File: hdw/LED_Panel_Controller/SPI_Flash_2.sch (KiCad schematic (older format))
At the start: 14 parts

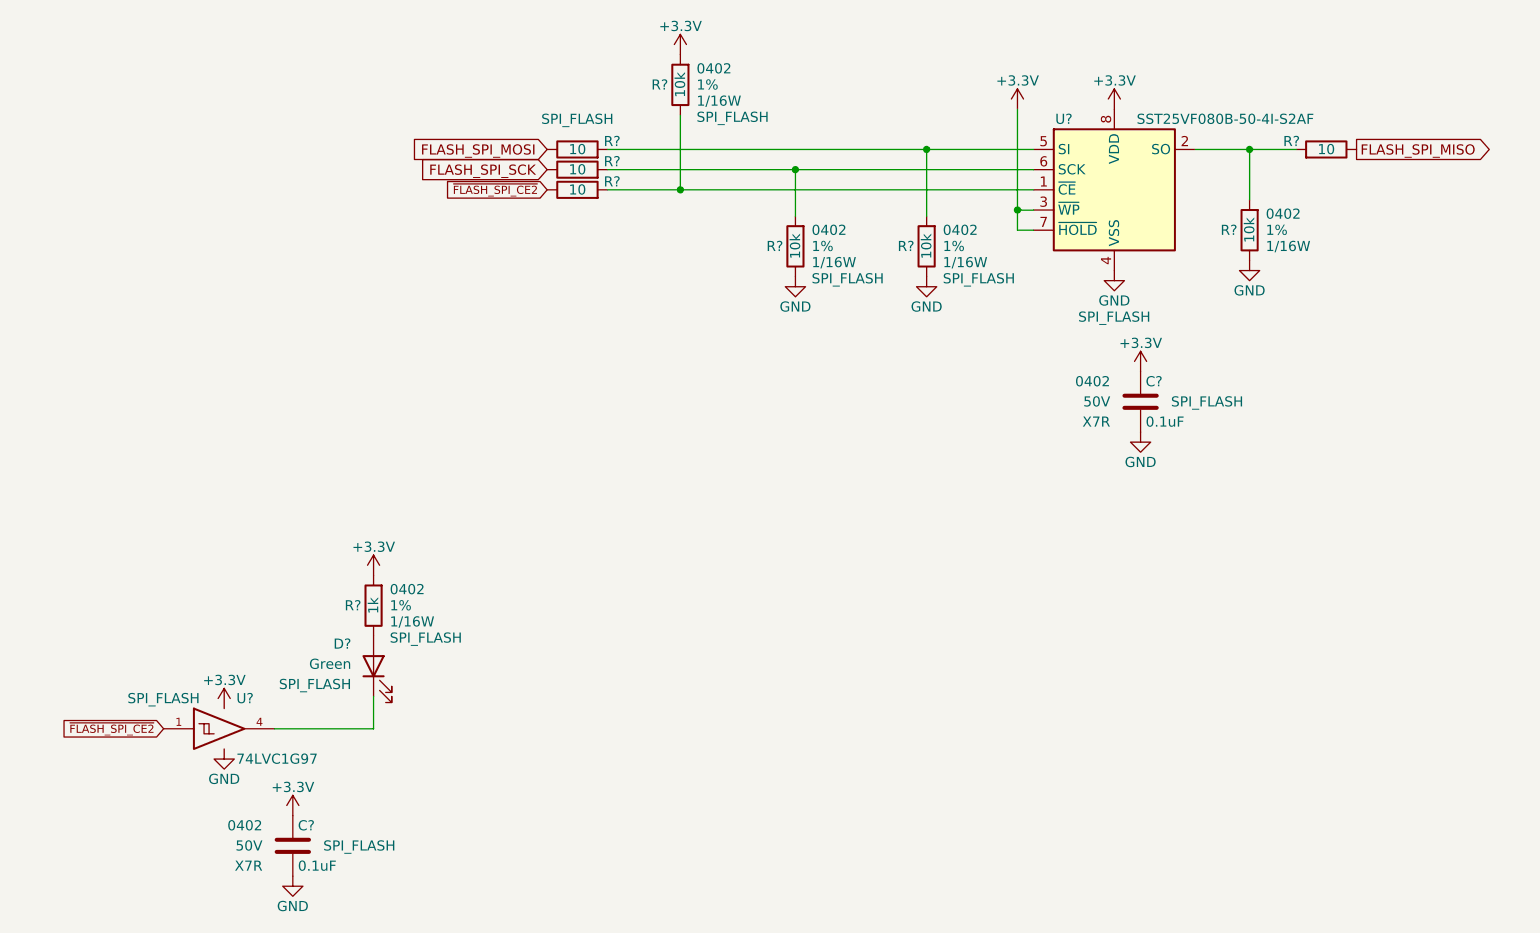
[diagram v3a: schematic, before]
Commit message: assigned I2C addresses
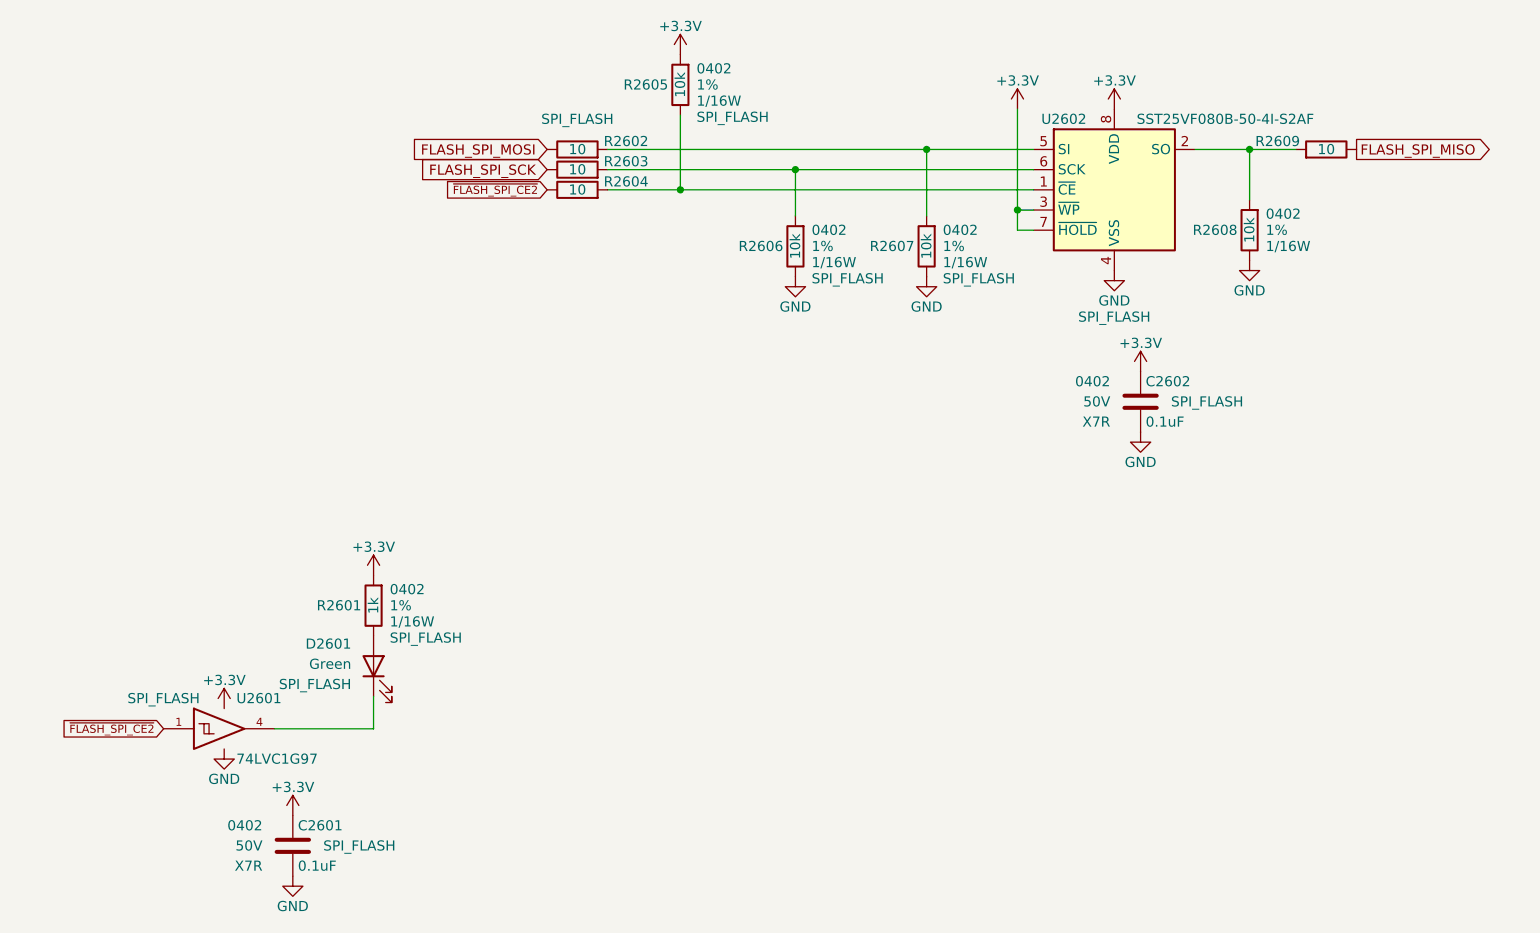
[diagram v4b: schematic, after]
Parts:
- removed C? (x2): 0.1uF, Capacitors_SMD:C_0402, symbol Custom_Library:C_Custom
- removed D?: Green, LEDs:LED_0402, symbol Device:LED
- removed R? (x2): 10k, Resistors_SMD:R_0402, symbol Custom_Library:R_Custom
- removed R? (x2): 10, Resistors_SMD:R_0402, symbol Custom_Library:R_Custom
- removed R?: 1k, Resistors_SMD:R_0402, symbol Custom_Library:R_Custom
- removed U?: SST25VF080B-50-4I-S2AF, Package_SO:SOIC-8_5.275x5.275mm_P1.27mm, symbol Memory_Flash:SST25VF080B-50-4x-S2Ax
- removed U?: 74LVC1G97, Package_TO_SOT_SMD:SOT-363_SC-70-6, symbol Custom_Library:74LVC1G97_Power_BUF
- added C2601, C2602: 0.1uF, Capacitors_SMD:C_0402, symbol Custom_Library:C_Custom
- added D2601: Green, LEDs:LED_0402, symbol Device:LED
- added R2601: 1k, Resistors_SMD:R_0402, symbol Custom_Library:R_Custom
- added R2604, R2609: 10, Resistors_SMD:R_0402, symbol Custom_Library:R_Custom
- added R2605, R2608: 10k, Resistors_SMD:R_0402, symbol Custom_Library:R_Custom
- added U2601: 74LVC1G97, Package_TO_SOT_SMD:SOT-363_SC-70-6, symbol Custom_Library:74LVC1G97_Power_BUF
- added U2602: SST25VF080B-50-4I-S2AF, Package_SO:SOIC-8_5.275x5.275mm_P1.27mm, symbol Memory_Flash:SST25VF080B-50-4x-S2Ax
- gave numbers to parts that had none: 4
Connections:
- net +3V3: now also C2601.1, C2602.1, R2601.1, R2605.1, U2601.5 (VCC), U2602.3 (~WP~), U2602.7 (~HOLD~), U2602.8 (VDD)
- net FLASH_SPI_MISO: now also R2609.2
- net GND: now also C2601.2, C2602.2, R2608.2, U2601.2 (GND), U2601.3 (GND), U2601.6 (GND), U2602.4 (VSS)
- net ~FLASH_SPI_CE2: now also R2604.2, U2601.1
- net at R2602.1, R2607.1: now also U2602.5 (SI)
- net at R2603.1, R2606.1: now also U2602.6 (SCK)
- new net: R2608.1, R2609.1, U2602.2 (SO)
- new net: D2601.1 (K), U2601.4
- new net: D2601.2 (A), R2601.2
- new net: R2604.1, R2605.2, U2602.1 (~CE)
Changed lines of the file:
@@
 $EndDescr
 $Comp
-L power:GND #PWR?
-U 1 1 5BB4E0E3
+L power:GND #PWR02611
+U 1 1 60786261
 P 6080 4050
-F 0 "#PWR?" H 6080 3800 50  0001 C CNN
+F 0 "#PWR02611" H 6080 3800 50  0001 C CNN
 F 1 "GND" H 6080 3900 50  0000 C CNN
 F 2 "" H 6080 4050 50  0001 C CNN
@@
 $EndComp
 $Comp
-L Custom_Library:R_Custom R?
-U 1 1 5BB4EDD1
+L Custom_Library:R_Custom R2608
+U 1 1 6078626A
 P 6750 3850
-F 0 "R?" H 6690 3850 50  0000 R CNN
+F 0 "R2608" H 6690 3850 50  0000 R CNN
 F 1 "10k" V 6750 3850 50  0000 C CNN
 F 2 "Resistors_SMD:R_0402" H 6750 3850 50  0001 C CNN
@@
 $EndComp
 $Comp
-L power:GND #PWR?
-U 1 1 5BB4EE63
+L power:GND #PWR02608
+U 1 1 6078626C
 P 5150 4080
-F 0 "#PWR?" H 5150 3830 50  0001 C CNN
+F 0 "#PWR02608" H 5150 3830 50  0001 C CNN
 F 1 "GND" H 5150 3930 50  0000 C CNN
 F 2 "" H 5150 4080 50  0001 C CNN
@@
 $EndComp
 $Comp
-L power:GND #PWR?
+L power:GND #PWR02614
 U 1 1 5BB4EE7C
 P 6750 4000
-F 0 "#PWR?" H 6750 3750 50  0001 C CNN
+F 0 "#PWR02614" H 6750 3750 50  0001 C CNN
 F 1 "GND" H 6750 3850 50  0000 C CNN
 F 2 "" H 6750 4000 50  0001 C CNN
@@
 $EndComp
 $Comp
-L Custom_Library:R_Custom R?
+L Custom_Library:R_Custom R2602
 U 1 1 5BB4F53B
 P 3420 3450
-F 0 "R?" V 3380 3580 50  0000 L CNN
+F 0 "R2602" V 3380 3580 50  0000 L CNN
 F 1 "10" V 3420 3450 50  0000 C CNN
 F 2 "Resistors_SMD:R_0402" H 3420 3450 50  0001 C CNN
@@
 	3570 3650 3930 3650
 $Comp
-L power:+3.3V #PWR?
-U 1 1 5BDF3D33
+L power:+3.3V #PWR02606
+U 1 1 60786285
 P 3930 2980
-F 0 "#PWR?" H 3930 2830 50  0001 C CNN
+F 0 "#PWR02606" H 3930 2830 50  0001 C CNN
 F 1 "+3.3V" H 3930 3120 50  0000 C CNN
 F 2 "" H 3930 2980 50  0001 C CNN
@@
 $EndComp
 $Comp
-L power:+3.3V #PWR?
-U 1 1 5BDF3DF4
+L power:+3.3V #PWR02610
+U 1 1 6078628C
 P 6080 3250
-F 0 "#PWR?" H 6080 3100 50  0001 C CNN
+F 0 "#PWR02610" H 6080 3100 50  0001 C CNN
 F 1 "+3.3V" H 6080 3390 50  0000 C CNN
 F 2 "" H 6080 3250 50  0001 C CNN
@@
 $Comp
 L Custom_Library:C_Custom C?
-U 1 1 5C15F697
+U 1 1 60786294
 P 2010 6900
-AR Path="/5BAAE16C/5C15F697" Ref="C?"  Part="1"
-AR Path="/5BB181D8/5C15F697" Ref="C?"  Part="1"
-AR Path="/5BB2595E/5C15F697" Ref="C?"  Part="1"
-AR Path="/5F583577/5C15F697" Ref="C?"  Part="1"
-AR Path="/5F583592/5C15F697" Ref="C?"  Part="1"
-F 0 "C?" H 2035 7000 50  0000 L CNN
+AR Path="/5BAAE16C/60786294" Ref="C?"  Part="1"
+AR Path="/5BB181D8/60786294" Ref="C?"  Part="1"
+AR Path="/5BB2595E/60786294" Ref="C?"  Part="1"
+AR Path="/5F583577/60786294" Ref="C?"  Part="1"
+AR Path="/5F583592/60786294" Ref="C2601"  Part="1"
+F 0 "C2601" H 2035 7000 50  0000 L CNN
 F 1 "0.1uF" H 2035 6800 50  0000 L CNN
 F 2 "Capacitors_SMD:C_0402" H 2048 6750 50  0001 C CNN
@@
 $EndComp
 $Comp
-L power:+3.3V #PWR?
-U 1 1 5C161B83
+L power:+3.3V #PWR02601
+U 1 1 6078629A
 P 1670 6220
-F 0 "#PWR?" H 1670 6070 50  0001 C CNN
+F 0 "#PWR02601" H 1670 6070 50  0001 C CNN
 F 1 "+3.3V" H 1670 6360 50  0000 C CNN
 F 2 "" H 1670 6220 50  0001 C CNN
@@
 $EndComp
 $Comp
-L power:+3.3V #PWR?
-U 1 1 5C161BE9
+L power:+3.3V #PWR02603
+U 1 1 6078629E
 P 2010 6750
-F 0 "#PWR?" H 2010 6600 50  0001 C CNN
+F 0 "#PWR02603" H 2010 6600 50  0001 C CNN
 F 1 "+3.3V" H 2010 6890 50  0000 C CNN
 F 2 "" H 2010 6750 50  0001 C CNN
@@
 $EndComp
 $Comp
-L power:GND #PWR?
-U 1 1 5C161C44
+L power:GND #PWR02604
+U 1 1 607862A7
 P 2010 7050
-F 0 "#PWR?" H 2010 6800 50  0001 C CNN
+F 0 "#PWR02604" H 2010 6800 50  0001 C CNN
 F 1 "GND" H 2010 6900 50  0000 C CNN
 F 2 "" H 2010 7050 50  0001 C CNN
@@
 $EndComp
 $Comp
-L power:GND #PWR?
-U 1 1 5C161C9F
+L power:GND #PWR02602
+U 1 1 607862AD
 P 1670 6420
-F 0 "#PWR?" H 1670 6170 50  0001 C CNN
+F 0 "#PWR02602" H 1670 6170 50  0001 C CNN
 F 1 "GND" H 1670 6270 50  0000 C CNN
 F 2 "" H 1670 6420 50  0001 C CNN
@@
 $Comp
 L power:+3.3V #PWR?
-U 1 1 5C166A81
+U 1 1 607862B7
 P 2410 5560
-AR Path="/5BB844FD/5C166A81" Ref="#PWR?"  Part="1"
-AR Path="/5BF346B3/5C166A81" Ref="#PWR?"  Part="1"
-AR Path="/5BB2595E/5C166A81" Ref="#PWR?"  Part="1"
-AR Path="/5F583577/5C166A81" Ref="#PWR?"  Part="1"
-AR Path="/5F583592/5C166A81" Ref="#PWR?"  Part="1"
-F 0 "#PWR?" H 2410 5410 50  0001 C CNN
+AR Path="/5BB844FD/607862B7" Ref="#PWR?"  Part="1"
+AR Path="/5BF346B3/607862B7" Ref="#PWR?"  Part="1"
+AR Path="/5BB2595E/607862B7" Ref="#PWR?"  Part="1"
+AR Path="/5F583577/607862B7" Ref="#PWR?"  Part="1"
+AR Path="/5F583592/607862B7" Ref="#PWR02605"  Part="1"
+F 0 "#PWR02605" H 2410 5410 50  0001 C CNN
 F 1 "+3.3V" H 2410 5700 50  0000 C CNN
 F 2 "" H 2410 5560 50  0001 C CNN
@@
 $Comp
 L Device:LED D?
-U 1 1 5C166A95
+U 1 1 607862B8
 P 2410 6010
-AR Path="/5BB844FD/5C166A95" Ref="D?"  Part="1"
-AR Path="/5BF346B3/5C166A95" Ref="D?"  Part="1"
-AR Path="/5BB2595E/5C166A95" Ref="D?"  Part="1"
-AR Path="/5F583577/5C166A95" Ref="D?"  Part="1"
-AR Path="/5F583592/5C166A95" Ref="D?"  Part="1"
-F 0 "D?" V 2520 6120 50  0000 L CNN
+AR Path="/5BB844FD/607862B8" Ref="D?"  Part="1"
+AR Path="/5BF346B3/607862B8" Ref="D?"  Part="1"
+AR Path="/5BB2595E/607862B8" Ref="D?"  Part="1"
+AR Path="/5F583577/607862B8" Ref="D?"  Part="1"
+AR Path="/5F583592/607862B8" Ref="D2601"  Part="1"
+F 0 "D2601" V 2520 6120 50  0000 L CNN
 F 1 "Green" V 2420 6120 50  0000 L CNN
 F 2 "LEDs:LED_0402" H 2410 6010 50  0001 C CNN
@@
 $EndComp
 $Comp
-L Memory_Flash:SST25VF080B-50-4x-S2Ax U?
-U 1 1 5F6879D5
+L Memory_Flash:SST25VF080B-50-4x-S2Ax U2602
+U 1 1 607862FA
 P 6080 3650
-F 0 "U?" H 5830 4000 50  0000 C CNN
+F 0 "U2602" H 5830 4000 50  0000 C CNN
 F 1 "SST25VF080B-50-4I-S2AF" H 6630 4000 50  0000 C CNN
 F 2 "Package_SO:SOIC-8_5.275x5.275mm_P1.27mm" H 6080 2950 50  0001 C CNN
@@
 $EndComp
 $Comp
-L power:+3.3V #PWR?
-U 1 1 5F689292
+L power:+3.3V #PWR02612
+U 1 1 607862FE
 P 6210 4550
-F 0 "#PWR?" H 6210 4400 50  0001 C CNN
+F 0 "#PWR02612" H 6210 4400 50  0001 C CNN
 F 1 "+3.3V" H 6210 4690 50  0000 C CNN
 F 2 "" H 6210 4550 50  0001 C CNN
@@
 $EndComp
 $Comp
-L power:GND #PWR?
+L power:GND #PWR02613
 U 1 1 5F689298
 P 6210 4850
-F 0 "#PWR?" H 6210 4600 50  0001 C CNN
+F 0 "#PWR02613" H 6210 4600 50  0001 C CNN
 F 1 "GND" H 6210 4700 50  0000 C CNN
 F 2 "" H 6210 4850 50  0001 C CNN
@@
 $EndComp
 $Comp
-L power:+3.3V #PWR?
-U 1 1 5F69329F
+L power:+3.3V #PWR02609
+U 1 1 6078630C
 P 5600 3250
-F 0 "#PWR?" H 5600 3100 50  0001 C CNN
+F 0 "#PWR02609" H 5600 3100 50  0001 C CNN
 F 1 "+3.3V" H 5600 3390 50  0000 C CNN
 F 2 "" H 5600 3250 50  0001 C CNN
@@
 	3570 3550 4500 3550
 $Comp
-L Custom_Library:R_Custom R?
+L Custom_Library:R_Custom R2606
 U 1 1 5F697048
 P 4500 3930
-F 0 "R?" H 4440 3930 50  0000 R CNN
+F 0 "R2606" H 4440 3930 50  0000 R CNN
 F 1 "10k" V 4500 3930 50  0000 C CNN
 F 2 "Resistors_SMD:R_0402" H 4500 3930 50  0001 C CNN
@@
 $EndComp
 $Comp
-L power:GND #PWR?
-U 1 1 5F697052
+L power:GND #PWR02607
+U 1 1 6078631F
 P 4500 4080
-F 0 "#PWR?" H 4500 3830 50  0001 C CNN
+F 0 "#PWR02607" H 4500 3830 50  0001 C CNN
 F 1 "GND" H 4500 3930 50  0000 C CNN
 F 2 "" H 4500 4080 50  0001 C CNN
@@
 	4500 3550 5680 3550
 $Comp
-L Custom_Library:R_Custom R?
+L Custom_Library:R_Custom R2603
 U 1 1 5F7379BB
 P 3420 3550
-F 0 "R?" V 3380 3680 50  0000 L CNN
+F 0 "R2603" V 3380 3680 50  0000 L CNN
 F 1 "10" V 3420 3550 50  0000 C CNN
 F 2 "Resistors_SMD:R_0402" H 3420 3550 50  0001 C CNN
@@
 $EndComp
 $Comp
-L Custom_Library:R_Custom R?
-U 1 1 5F737B74
+L Custom_Library:R_Custom R2604
+U 1 1 6078632B
 P 3420 3650
-F 0 "R?" V 3380 3780 50  0000 L CNN
+F 0 "R2604" V 3380 3780 50  0000 L CNN
 F 1 "10" V 3420 3650 50  0000 C CNN
 F 2 "Resistors_SMD:R_0402" H 3420 3650 50  0001 C CNN
@@
 $EndComp
 $Comp
-L Custom_Library:R_Custom R?
-U 1 1 5F737D15
+L Custom_Library:R_Custom R2609
+U 1 1 60786331
 P 7130 3450
-F 0 "R?" V 7090 3580 50  0000 L CNN
+F 0 "R2609" V 7090 3580 50  0000 L CNN
 F 1 "10" V 7130 3450 50  0000 C CNN
 F 2 "Resistors_SMD:R_0402" H 7130 3450 50  0001 C CNN
@@
 $EndComp
 $Comp
-L Custom_Library:74LVC1G97_Power_BUF U?
-U 1 1 5FE9D8D5
+L Custom_Library:74LVC1G97_Power_BUF U2601
+U 1 1 60786345
 P 1670 6320
-F 0 "U?" H 1730 6470 50  0000 L CNN
+F 0 "U2601" H 1730 6470 50  0000 L CNN
 F 1 "74LVC1G97" H 1730 6170 50  0000 L CNN
 F 2 "Package_TO_SOT_SMD:SOT-363_SC-70-6" H 1720 6320 50  0001 C CNN
@@
 $EndComp
 $Comp
-L Custom_Library:R_Custom R?
+L Custom_Library:R_Custom R2607
 U 1 1 6026393A
 P 5150 3930
-F 0 "R?" H 5090 3930 50  0000 R CNN
+F 0 "R2607" H 5090 3930 50  0000 R CNN
 F 1 "10k" V 5150 3930 50  0000 C CNN
 F 2 "Resistors_SMD:R_0402" H 5150 3930 50  0001 C CNN
@@
 $EndComp
 $Comp
-L Custom_Library:R_Custom R?
-U 1 1 60263FB7
+L Custom_Library:R_Custom R2605
+U 1 1 60786362
 P 3930 3130
-F 0 "R?" H 3870 3130 50  0000 R CNN
+F 0 "R2605" H 3870 3130 50  0000 R CNN
 F 1 "10k" V 3930 3130 50  0000 C CNN
 F 2 "Resistors_SMD:R_0402" H 3930 3130 50  0001 C CNN
@@
 $EndComp
 $Comp
-L Custom_Library:R_Custom R?
-U 1 1 60266213
+L Custom_Library:R_Custom R2601
+U 1 1 60786366
 P 2410 5710
-F 0 "R?" H 2350 5710 50  0000 R CNN
+F 0 "R2601" H 2350 5710 50  0000 R CNN
 F 1 "1k" V 2410 5710 50  0000 C CNN
 F 2 "Resistors_SMD:R_0402" H 2410 5710 50  0001 C CNN
@@
 $Comp
 L Custom_Library:C_Custom C?
-U 1 1 60269564
+U 1 1 6078636B
 P 6210 4700
-AR Path="/5BAAE16C/60269564" Ref="C?"  Part="1"
-AR Path="/5BB181D8/60269564" Ref="C?"  Part="1"
-AR Path="/5BB2595E/60269564" Ref="C?"  Part="1"
-AR Path="/5F583577/60269564" Ref="C?"  Part="1"
-AR Path="/5F583592/60269564" Ref="C?"  Part="1"
-F 0 "C?" H 6235 4800 50  0000 L CNN
+AR Path="/5BAAE16C/6078636B" Ref="C?"  Part="1"
+AR Path="/5BB181D8/6078636B" Ref="C?"  Part="1"
+AR Path="/5BB2595E/6078636B" Ref="C?"  Part="1"
+AR Path="/5F583577/6078636B" Ref="C?"  Part="1"
+AR Path="/5F583592/6078636B" Ref="C2602"  Part="1"
+F 0 "C2602" H 6235 4800 50  0000 L CNN
 F 1 "0.1uF" H 6235 4600 50  0000 L CNN
 F 2 "Capacitors_SMD:C_0402" H 6248 4550 50  0001 C CNN
